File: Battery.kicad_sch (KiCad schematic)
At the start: 14 parts, among them J1 Keystone-1042, J2 Keystone-1042, J3 Keystone-1042, J4 Keystone-1042, J5 Keystone-1042, J6 Keystone-1042

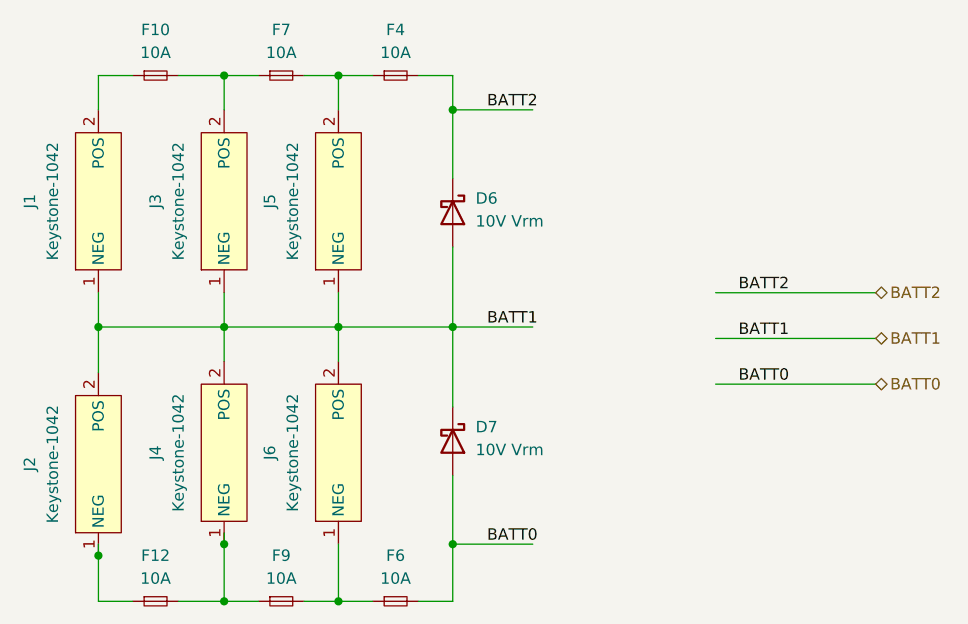
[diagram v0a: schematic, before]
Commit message: Updated footprint to follow PC/104
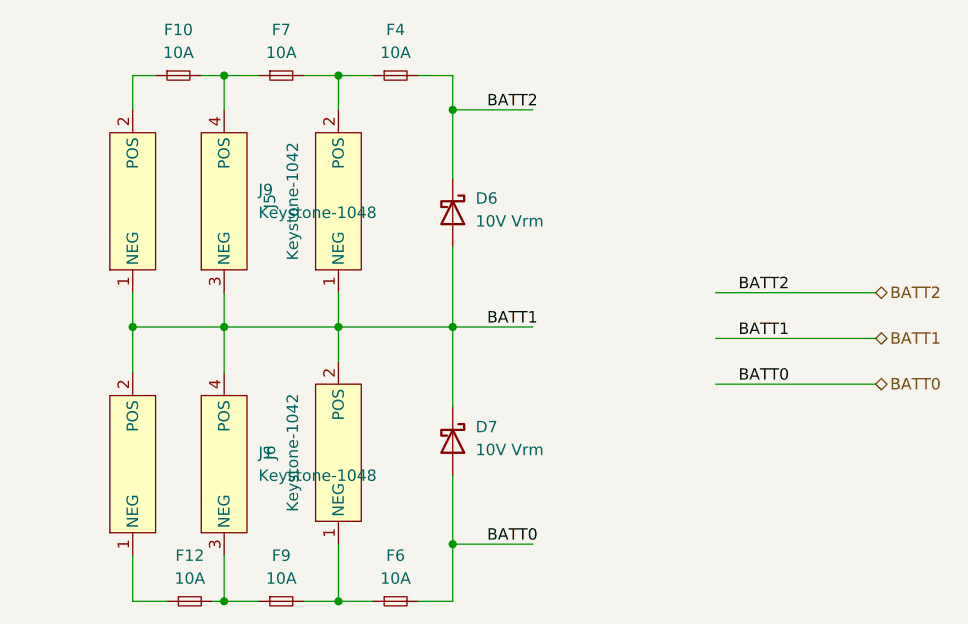
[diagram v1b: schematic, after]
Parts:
- removed J1, J2, J3, J4: Keystone-1042, Battery-Board:Keystone_1042, symbol Battery-Board:Keystone-1042
- added J1, J9: Keystone-1048, Battery-Board:BAT_1048, symbol Battery-Board:Keystone-1048
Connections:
- net BATT1: now also J1.2 (POS), J1.4 (POS), J9.1 (NEG), J9.3 (NEG)
- net at F12.2, F9.1: now also J1.3 (NEG)
- net at F12.1: now also J1.1 (NEG)
- net at F10.1: now also J9.2 (POS)
- net at F10.2, F7.1: now also J9.4 (POS)
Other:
- moved on the sheet: F10, F12
